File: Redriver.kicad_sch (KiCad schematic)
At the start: 100 parts, among them U1 DS320PR810NJXR, U2 DS320PR810NJXR

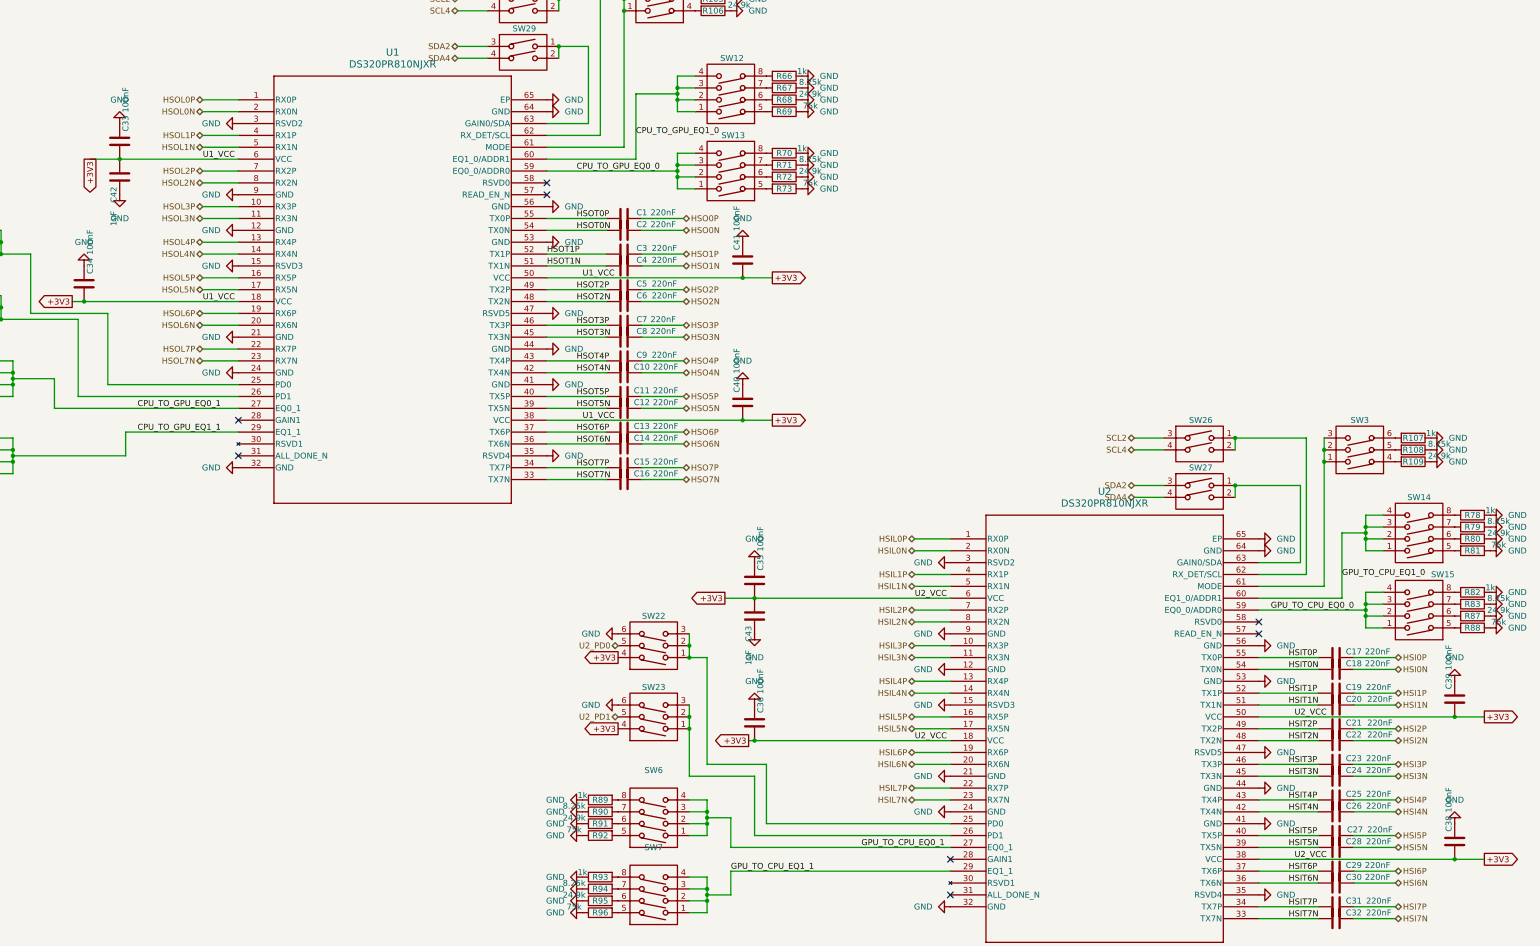
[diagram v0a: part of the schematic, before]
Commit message: added more decoupling caps
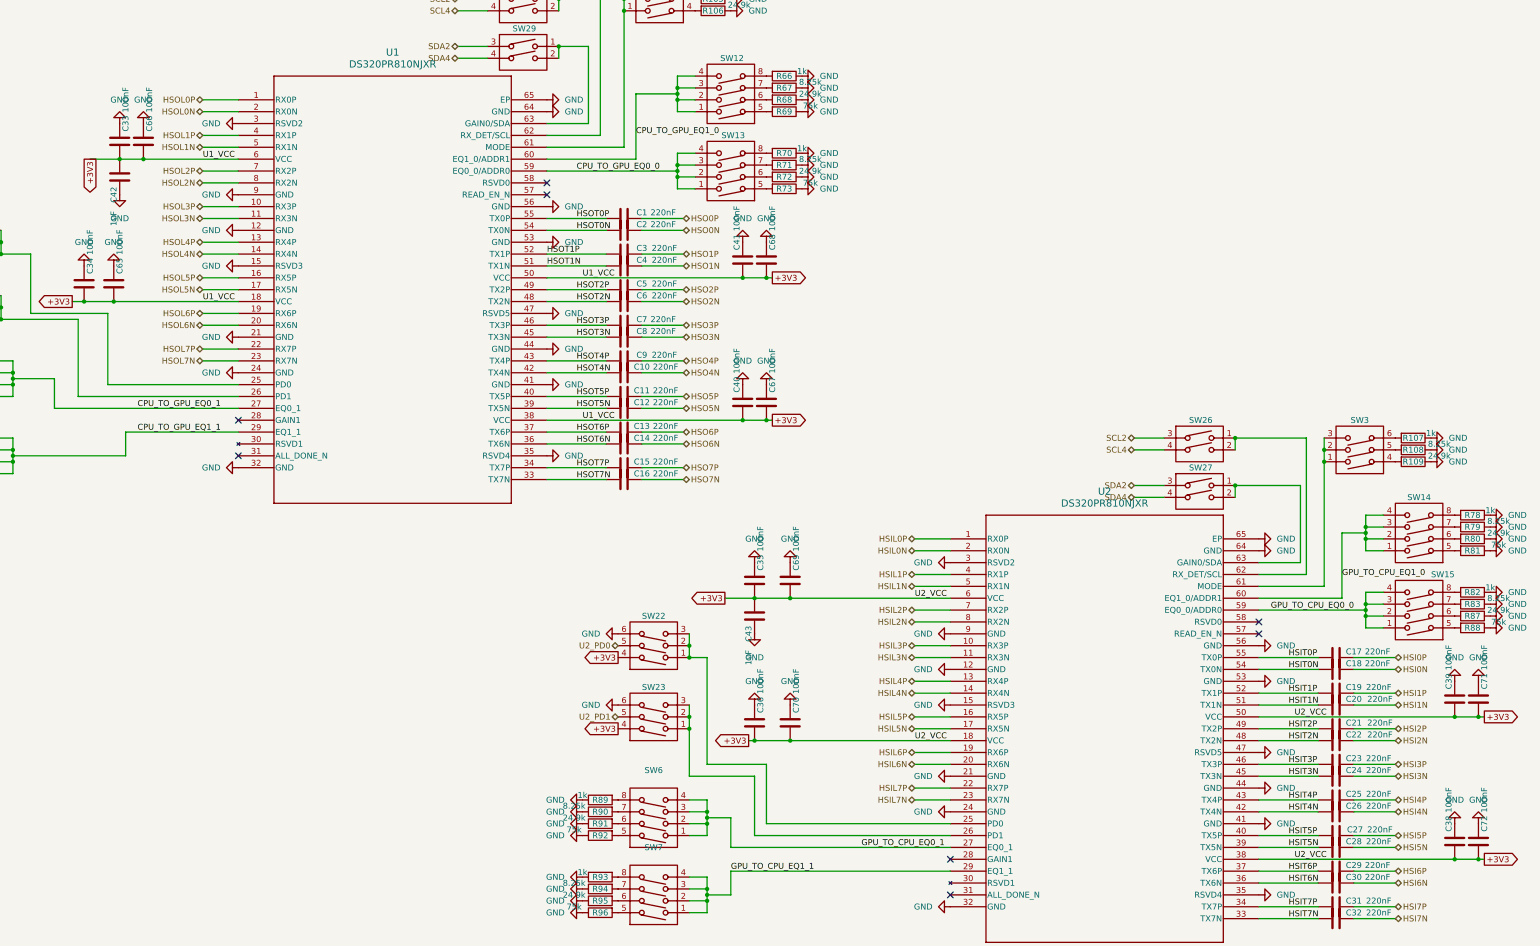
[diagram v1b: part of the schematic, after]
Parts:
- added C65, C66, C67, C68, C69, C70, C71, C72: 100nF, Capacitor_SMD:C_0201_0603Metric, symbol Device:C
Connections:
- net +3V3: now also C65.2, C66.2, C67.2, C68.2, C69.2, C70.2, C71.2, C72.2
- net GND: now also C65.1, C66.1, C67.1, C68.1, C69.1, C70.1, C71.1, C72.1

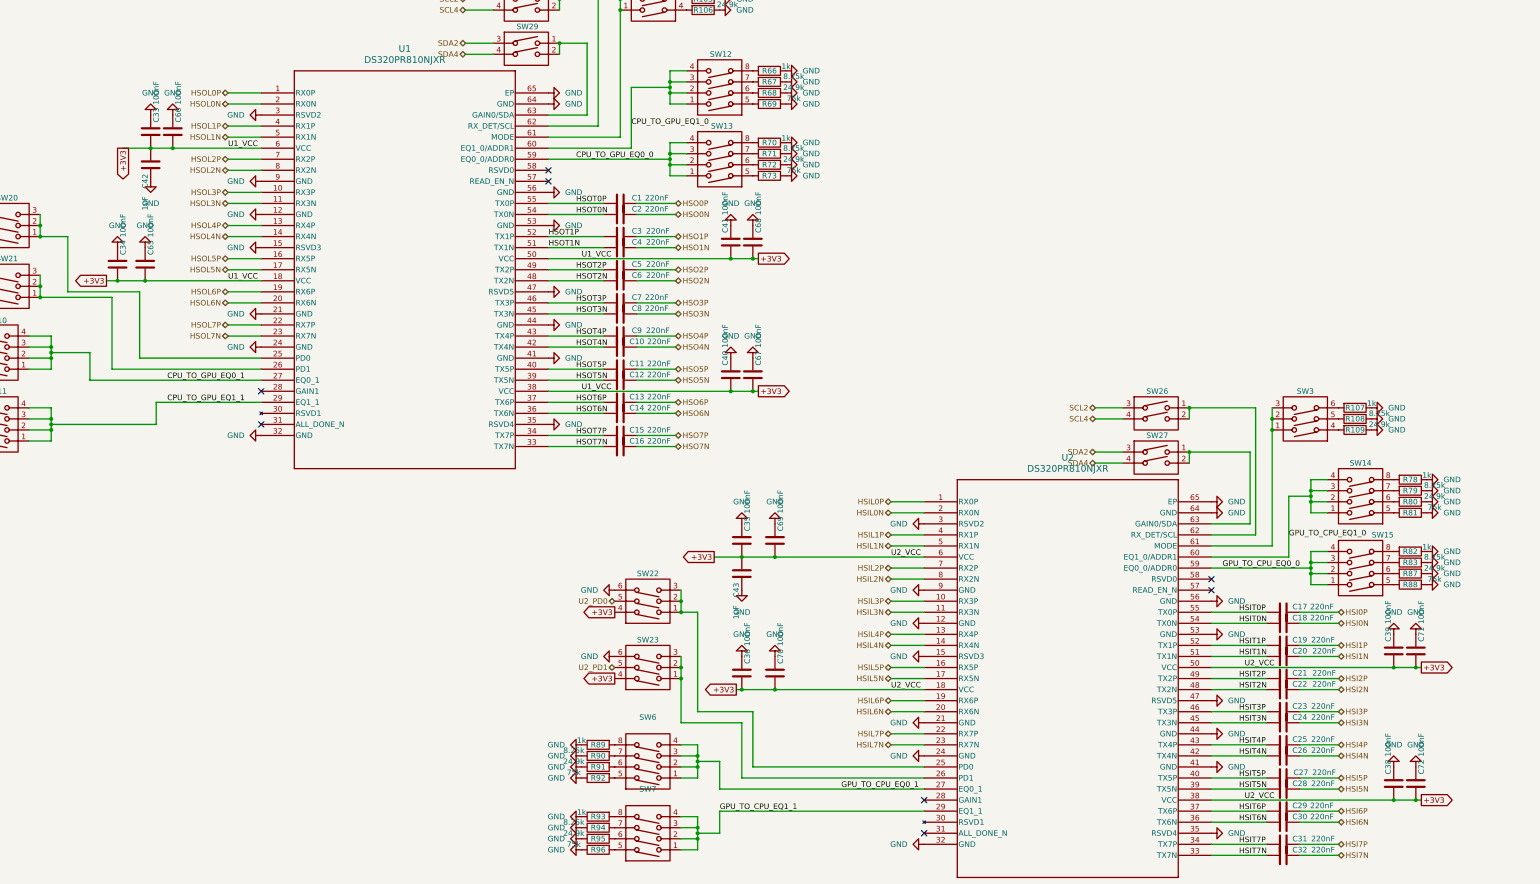
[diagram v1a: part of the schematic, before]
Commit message: added more decoupling caps
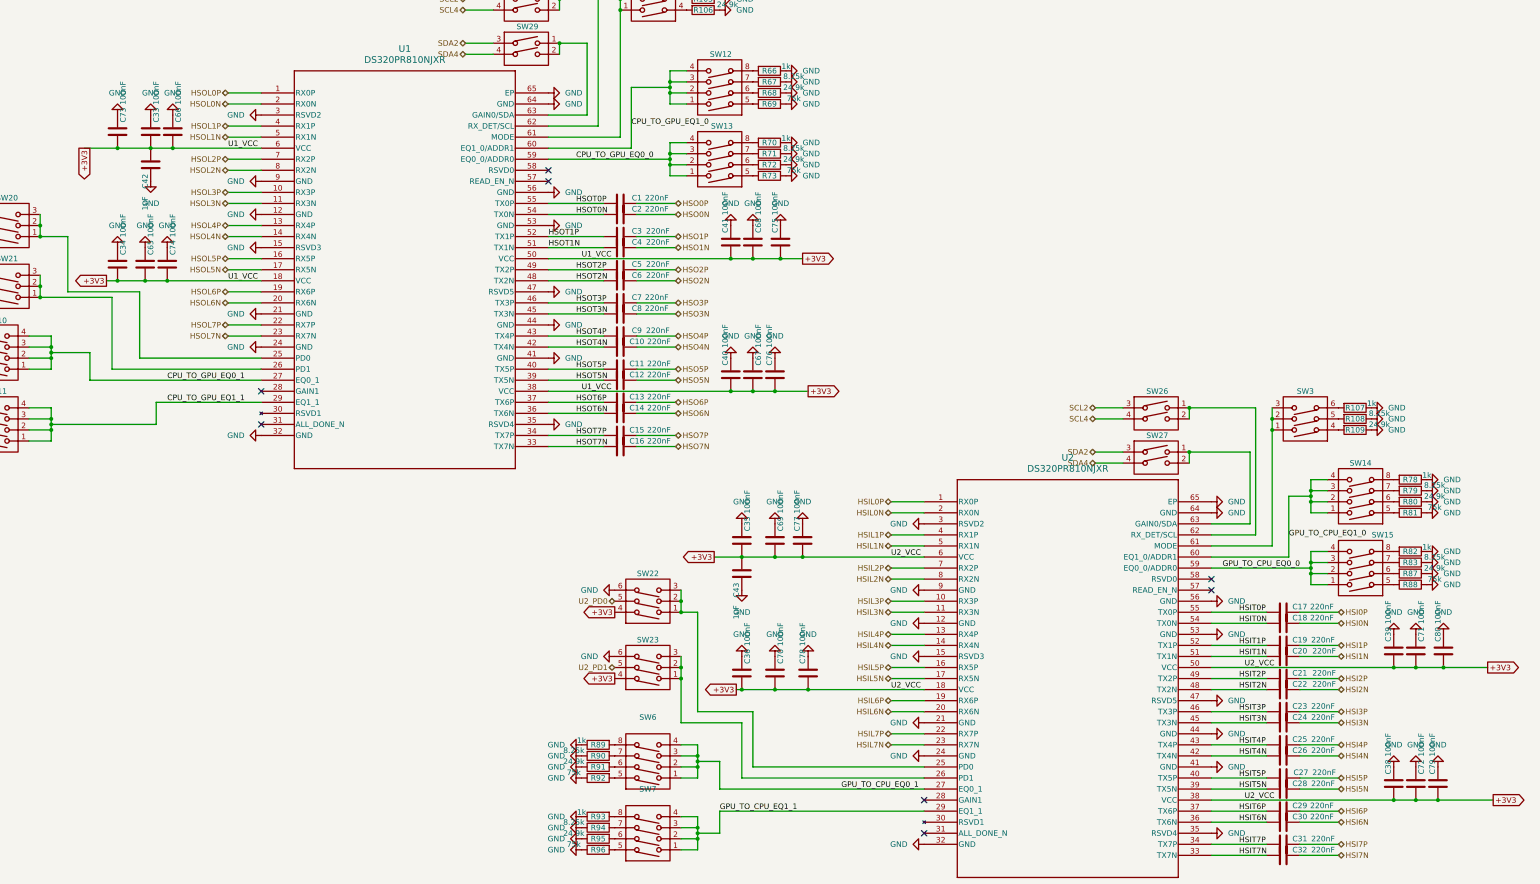
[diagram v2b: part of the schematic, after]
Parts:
- added C73, C74, C75, C76, C77, C78, C79, C80: 100nF, Capacitor_SMD:C_0201_0603Metric, symbol Device:C
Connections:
- net +3V3: now also C73.2, C74.2, C75.2, C76.2, C77.2, C78.2, C79.2, C80.2
- net GND: now also C73.1, C74.1, C75.1, C76.1, C77.1, C78.1, C79.1, C80.1

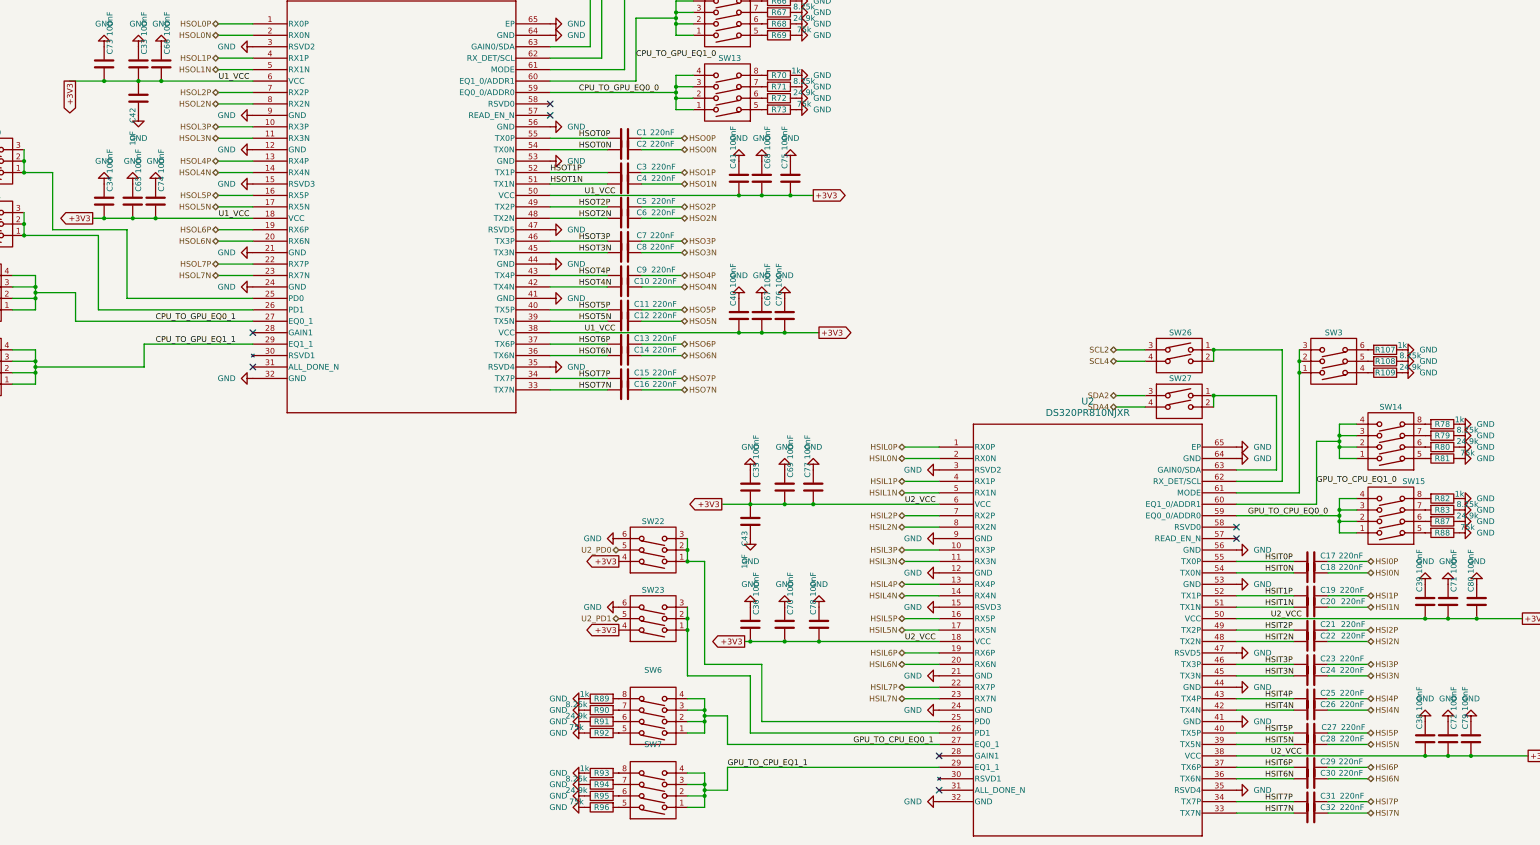
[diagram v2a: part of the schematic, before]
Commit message: added more decoupling caps
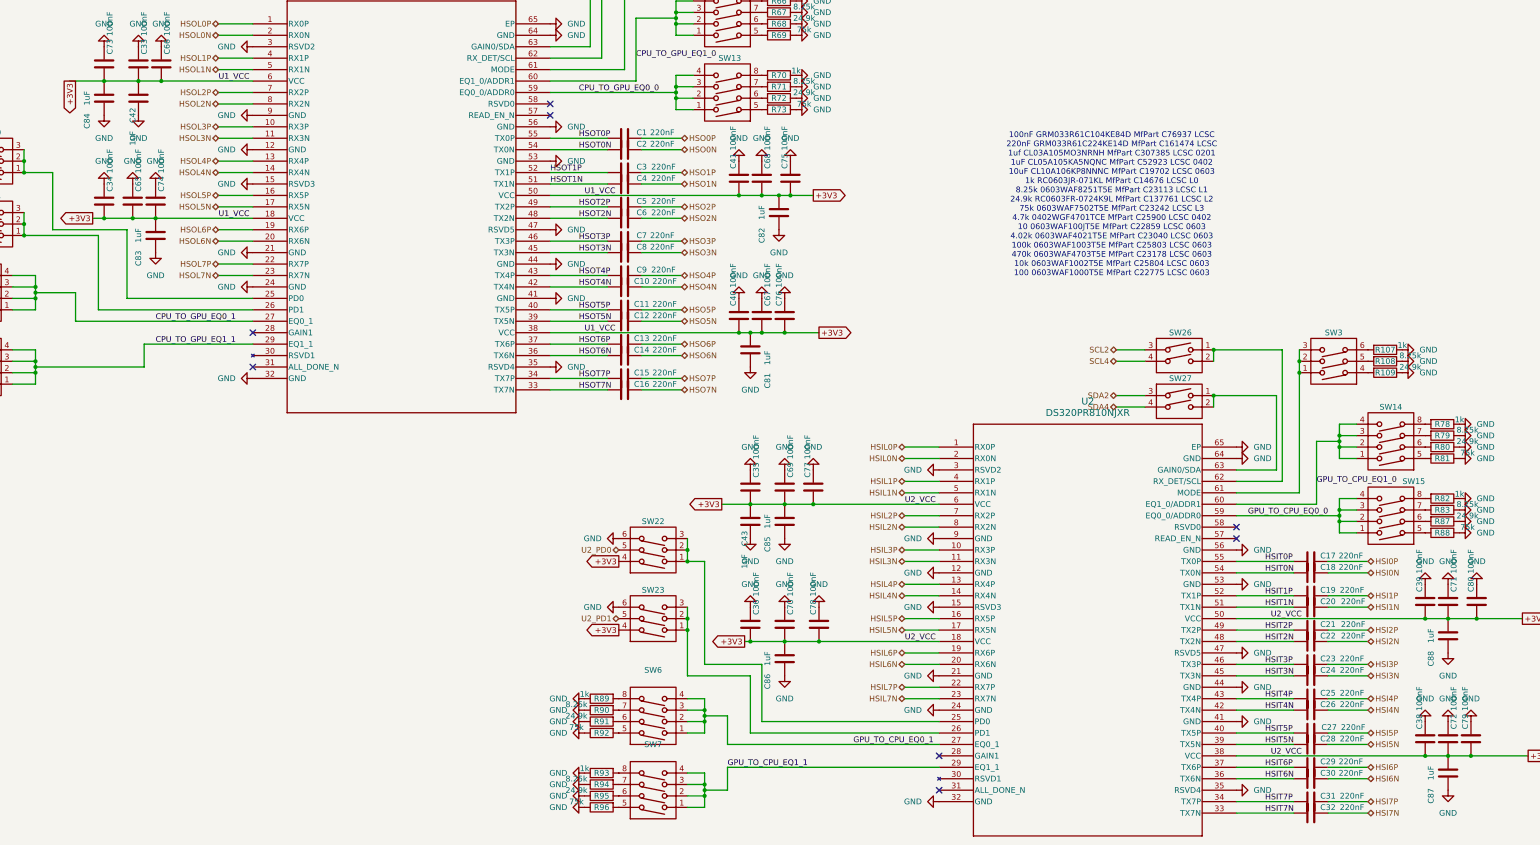
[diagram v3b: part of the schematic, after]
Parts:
- added C81, C82, C83, C84, C85, C86, C87, C88: 1uF, Capacitor_SMD:C_0402_1005Metric, symbol Device:C
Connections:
- net +3V3: now also C81.1, C82.1, C83.1, C84.1, C85.1, C86.1, C87.1, C88.1
- net GND: now also C81.2, C82.2, C83.2, C84.2, C85.2, C86.2, C87.2, C88.2
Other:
- note added: "100nF GRM033R61C104KE84D MfPart C76937 LCSC 220nF GRM033R61C224KE14D MfPart C161474 LCSC 1uf CL03A105MO3NRNH MfPart C307385 LCSC 0201 1uF CL05A105KA5NQNC MfPart C52923 LCSC 0402 10uF CL10A106KP8NNNC MfPart C19702 LCSC 0603 1k RC0603JR-071KL MfPart C14676 LCSC L0 8.25k 0603WAF8251T5E MfPart C23113 LCSC L1 24.9k RC0603FR-0724K9L MfPart C137761 LCSC L2 75k 0603WAF7502T5E MfPart C23242 LCSC L3 4.7k 0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"

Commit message: added more power rails on new layers
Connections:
- net +3V3: no longer C33.2, C34.2, C35.2, C36.2, C38.2, C39.2, C40.2, C41.2, C42.2, C43.2, C65.2, C66.2, C67.2, C68.2, C69.2, C70.2, C71.2, C72.2, C73.2, C74.2, C75.2, C76.2, C77.2, C78.2, C79.2, C80.2, C81.1, C82.1, C83.1, C84.1, C85.1, C86.1, C87.1, C88.1, U1.18 (VCC), U1.38 (VCC), U1.50 (VCC), U1.6 (VCC), U2.18 (VCC), U2.38 (VCC), U2.50 (VCC), U2.6 (VCC)
- new net +3V3Redriver: C33.2, C34.2, C35.2, C36.2, C38.2, C39.2, C40.2, C41.2, C42.2, C43.2, C65.2, C66.2, C67.2, C68.2, C69.2, C70.2, C71.2, C72.2, C73.2, C74.2, C75.2, C76.2, C77.2, C78.2, C79.2, C80.2, C81.1, C82.1, C83.1, C84.1, C85.1, C86.1, C87.1, C88.1, U1.18 (VCC), U1.38 (VCC), U1.50 (VCC), U1.6 (VCC), U2.18 (VCC), U2.38 (VCC), U2.50 (VCC), U2.6 (VCC)
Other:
- moved on the sheet: R100, R101, R102, R103, R104, R89, R90, R91, R92, R93, R94, R95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
